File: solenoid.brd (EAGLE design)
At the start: 76.2 x 25.4 mm, 41 parts, among them Y1 ECS-80-S-4X

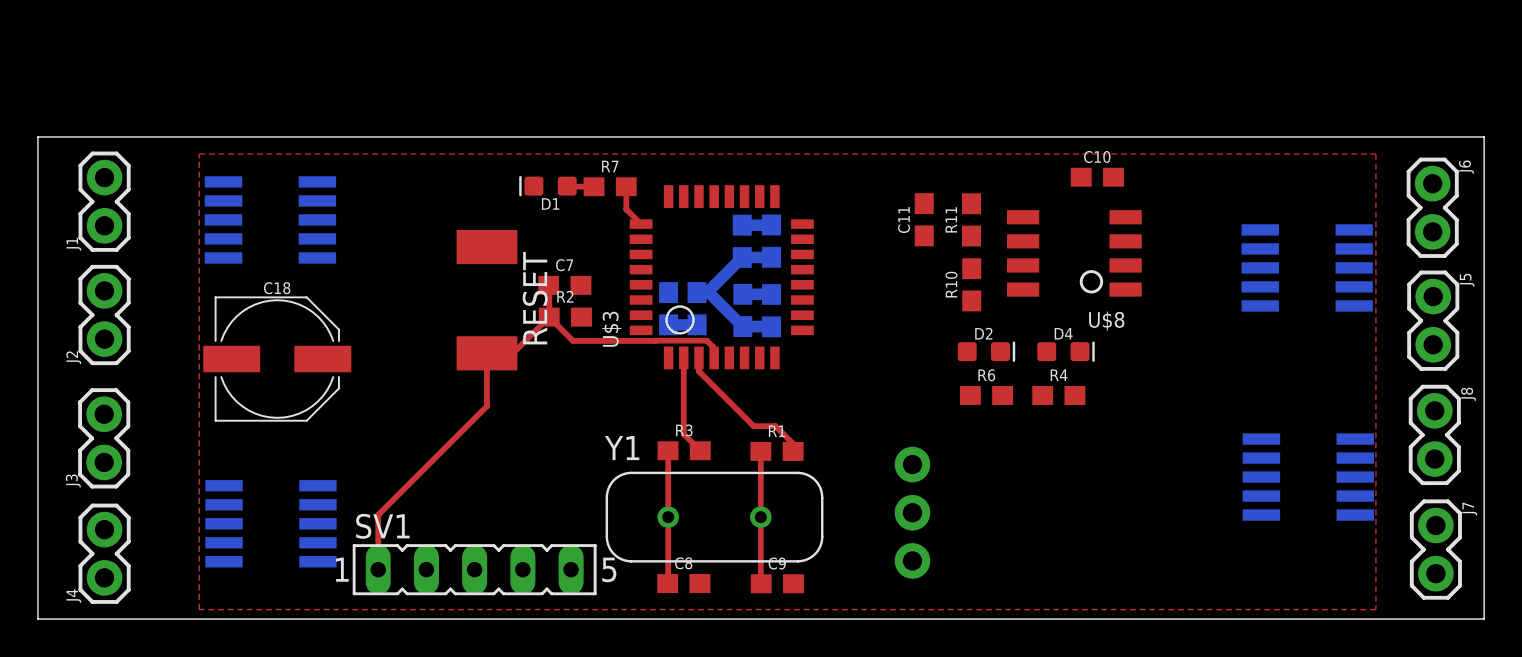
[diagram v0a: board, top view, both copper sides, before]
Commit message: Newly sized board w/ schematic changes
This is the first attempt at routing the 1.2" by  1.4" solenoid board with a removed h-bridge and with some questions as to some airwires
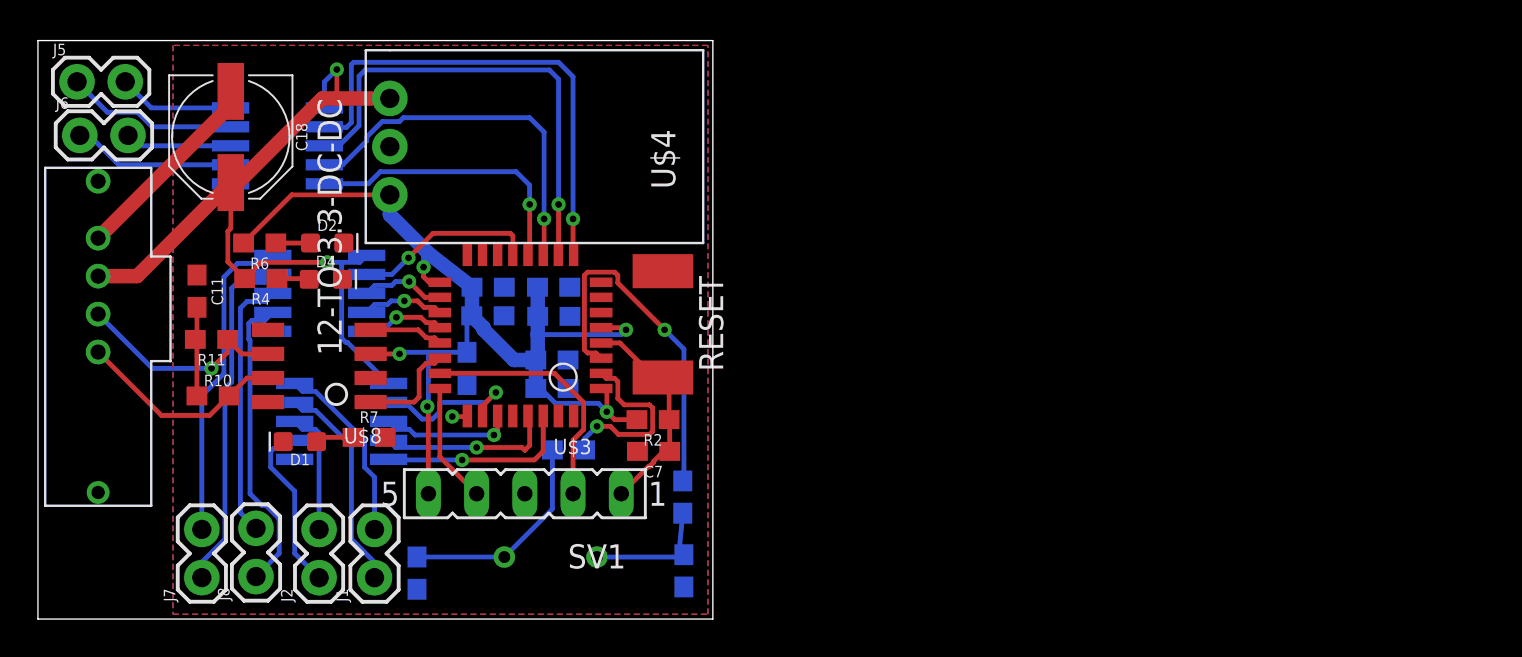
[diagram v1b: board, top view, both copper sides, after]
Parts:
- removed J3, J4: (no value), SparkFun-Connectors:1X02
- removed U$2: LV8548M, HBridge:SOP100P600X175-10N
- added U$7: T2I, BackplaneParts:T2I
- moved J5 72.4 mm to (2.06, 28.3), turned to 0 degrees
- moved J6 71.3 mm to (2.21, 25.5), turned to 0 degrees
- moved J7 65.1 mm to (8.64, 2.18), turned to 90 degrees
- moved J8 62.7 mm to (11.5, 2.24), turned to 90 degrees
- moved U$5 54.6 mm to (12.6, 24.9), turned to 0 degrees
- moved U$6 53.0 mm to (14.8, 17.2), turned to 0 degrees
- moved R4 42.5 mm to (11.7, 17.9), turned to 180 degrees
- moved R11 40.5 mm to (9.14, 14.7), turned to 180 degrees
- moved R10 40.4 mm to (9.23, 11.8), turned to 0 degrees
- moved U$8 40.2 mm to (17.5, 15.2)
- moved R6 39.1 mm to (11.7, 19.8), turned to 180 degrees
- moved D4 39.0 mm to (15.2, 17.9)
- moved C11 38.5 mm to (8.38, 17.3), turned to 270 degrees
- moved D2 35.1 mm to (15.2, 19.8)
- moved C10 34.7 mm to (22.6, 13.2), flipped to the bottom, turned to 270 degrees
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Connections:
- removed net GPIO4: U$2.IN1, U$3.PB5
- removed net GPIO5: U$2.IN2, U$3.PA0
- removed net GPIO6: U$2.IN3, U$3.PA1
- removed net GPIO7: U$2.IN4, U$3.PA2
- removed net SOL3_1: J3.2, U$2.OUT1
- removed net SOL3_2: J3.1, U$2.OUT2
- removed net SOL4_1: J4.2, U$2.OUT3
- removed net SOL4_2: J4.1, U$2.OUT4
- net 12V: now also U$7.3; no longer U$2.VCC
- net CAN_H: now also U$7.1
- net CAN_L: now also U$7.2
- net GND: now also U$7.4; no longer U$2.GND
- net GPIO0: now also U$1.IN4; no longer U$1.IN1
- net GPIO1: now also U$1.IN3; no longer U$1.IN2
- net GPIO2: now also U$1.IN2; no longer U$1.IN3
- net GPIO3: now also U$1.IN1; no longer U$1.IN4
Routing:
- net +3V3: track 9.36 -> 57.6 mm, vias 0 -> 5
- net 12V: track 0.00 -> 43.0 mm, vias 0 -> 2
- net GPIO8: track 0.00 -> 26.0 mm, vias 0 -> 1
- net GPIO9: track 0.00 -> 25.0 mm, vias 0 -> 1
- net GPIO10: track 0.00 -> 19.5 mm, vias 0 -> 1
- net SOL7_2: track 0.00 -> 18.4 mm
- net NRST: track 29.4 -> 11.6 mm
- net SOL7_1: track 0.00 -> 16.8 mm
- net SOL8_2: track 0.00 -> 16.1 mm
- net GPIO11: track 0.00 -> 15.1 mm, vias 0 -> 1
- net SOL8_1: track 0.00 -> 14.0 mm
- net SWDIO: track 0.00 -> 13.3 mm
- net OSC_OUT: track 7.65 -> 19.2 mm, vias 0 -> 1
- net CAN_L: track 0.00 -> 11.5 mm, vias 0 -> 1
- net SOL1_2: track 0.00 -> 11.4 mm
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- added copper zone on layer 16, net GND
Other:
- board size 76.2 x 25.4 mm -> 35.6 x 30.5 mm

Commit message: last version of this board
abandon all hope of this first draft. It passed DRC for default but not the DRC for ECE Senior Design have to scrap this idea :(
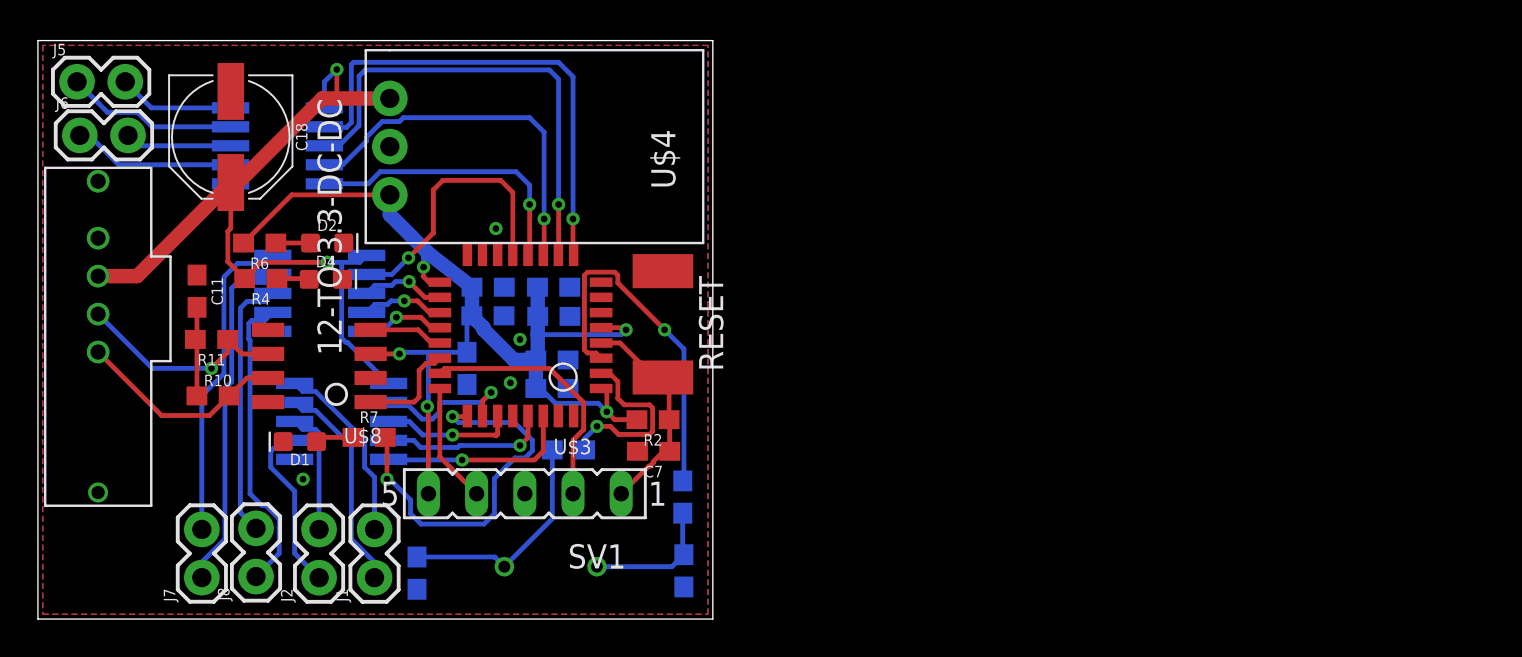
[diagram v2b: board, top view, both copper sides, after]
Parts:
- moved Y1 0.51 mm to (27.0, 2.76)
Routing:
- net LED: track 1.15 -> 20.1 mm, vias 1 -> 2
- net GND: track 10.6 -> 0.00 mm, vias 0 -> 4
- net GPIO12: track 9.64 -> 14.6 mm
- net N$2: track 11.3 -> 12.0 mm

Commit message: Clearance issues fixed
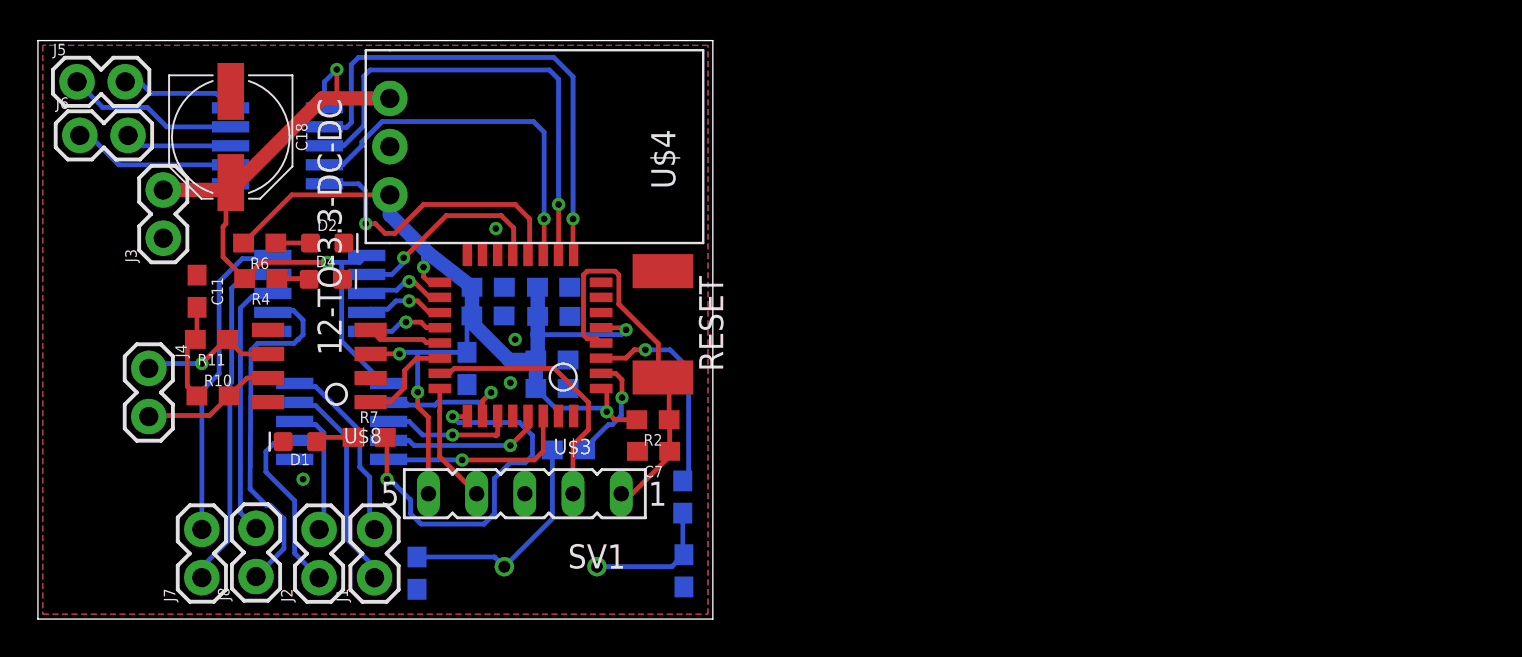
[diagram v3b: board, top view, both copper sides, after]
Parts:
- removed U$7: T2I, BackplaneParts:T2I
- added J3, J4: (no value), SparkFun-Connectors:1X02
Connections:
- net 12V: now also J3.2; no longer U$7.3
- net CAN_H: now also J4.2; no longer U$7.1
- net CAN_L: now also J4.1; no longer U$7.2
- net GND: now also J3.1; no longer U$7.4
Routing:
- net NRST: track 11.6 -> 20.4 mm
- net OSC_OUT: track 19.2 -> 11.3 mm
- net 12V: track 43.0 -> 37.8 mm
- net CAN_L: track 11.5 -> 7.23 mm
- net CAN_H: track 11.2 -> 7.13 mm
- net OSC_IN: track 9.91 -> 5.90 mm
- net GPIO12: track 14.6 -> 10.9 mm
- net SOL8_2: track 16.1 -> 18.5 mm
- net GPIO3: track 8.06 -> 7.23 mm
- net GPIO11: track 15.1 -> 15.8 mm

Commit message: Update solenoid.brd
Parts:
- moved J5 26.0 mm to (2.43, 2.31), turned to 90 degrees
- moved J6 20.8 mm to (5.51, 4.91), turned to 270 degrees
- moved U$5 0.76 mm to (11.9, 24.9)
- moved RESET 0.25 mm to (32.9, 15.8)
- moved J3 0.25 mm to (6.35, 20.1)
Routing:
- net SOL5_1: track 6.12 -> 30.9 mm
- net SOL6_1: track 5.63 -> 30.4 mm
- net SOL5_2: track 9.07 -> 32.6 mm
- net SOL6_2: track 8.58 -> 25.8 mm
- net GPIO10: track 19.3 -> 18.0 mm
- net OSC_OUT: track 11.3 -> 12.5 mm
- net SWCLK: track 6.36 -> 7.57 mm
- net GPIO9: track 25.0 -> 25.7 mm
- net +3V3: track 57.9 -> 58.5 mm
- net GPIO8: track 26.2 -> 26.8 mm
- net GPIO11: track 15.8 -> 16.3 mm

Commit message: Update solenoid.brd
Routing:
- net GND: track 0.00 -> 7.00 mm
- net SOL8_2: track 18.5 -> 20.4 mm
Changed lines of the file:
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@@
 <via x="24.13" y="20.574" extent="1-16" drill="0.35"/>
 <via x="25.146" y="14.732" extent="1-16" drill="0.35"/>
+<contactref element="J3" pad="1"/>
+<via x="13.97" y="15.24" extent="1-16" drill="0.35"/>
 <via x="24.892" y="12.446" extent="1-16" drill="0.35"/>
-<contactref element="J3" pad="1"/>
-<via x="14.478" y="16.51" extent="1-16" drill="0.35"/>
-<wire x1="14.478" y1="16.51" x2="12.3746" y2="15.158" width="0" layer="19" extent="16-16"/>
-<wire x1="22.606" y1="12.358" x2="24.892" y2="12.446" width="0" layer="19" extent="16-16"/>
+<wire x1="24.892" y1="12.446" x2="27.178" y2="12.446" width="0.2032" layer="1"/>
+<wire x1="28.224" y1="11.4" x2="28.224" y2="10.698" width="0.2032" layer="1"/>
+<wire x1="27.178" y1="12.446" x2="28.224" y2="11.4" width="0.2032" layer="1"/>
+<wire x1="24.892" y1="12.446" x2="24.638" y2="12.7" width="0.254" layer="16"/>
+<wire x1="24.638" y1="12.7" x2="22.948" y2="12.7" width="0.254" layer="16"/>
+<wire x1="22.948" y1="12.7" x2="22.606" y2="12.358" width="0.254" layer="16"/>
+<wire x1="28.022" y1="17.484" x2="32.931" y2="18.584" width="0" layer="19" extent="1-16"/>
+<wire x1="28.032" y1="15.946" x2="28.022" y2="17.484" width="0" layer="19" extent="16-16"/>
+<wire x1="27.934" y1="13.648" x2="28.032" y2="15.946" width="0" layer="19" extent="16-16"/>
+<wire x1="27.934" y1="12.148" x2="27.934" y2="13.648" width="0" layer="19" extent="16-16"/>
+<wire x1="28.224" y1="10.698" x2="27.934" y2="12.148" width="0" layer="19" extent="1-16"/>
+<wire x1="27.424" y1="10.698" x2="28.224" y2="10.698" width="0" layer="19" extent="1-1"/>
+<wire x1="25.146" y1="14.732" x2="24.638" y2="12.7" width="0" layer="19" extent="1-1"/>
+<wire x1="24.56" y1="15.976" x2="25.146" y2="14.732" width="0" layer="19" extent="16-16"/>
+<wire x1="24.57" y1="17.484" x2="24.56" y2="15.976" width="0" layer="19" extent="16-16"/>
+<wire x1="22.624" y1="19.198" x2="24.57" y2="17.484" width="0" layer="19" extent="1-16"/>
+<wire x1="24.13" y1="20.574" x2="22.624" y2="19.198" width="0" layer="19" extent="1-1"/>
+<wire x1="31.588" y1="8.836" x2="28.224" y2="10.698" width="0" layer="19" extent="1-1"/>
+<wire x1="25.654" y1="6.604" x2="27.424" y2="10.698" width="0" layer="19" extent="1-1"/>
+<wire x1="17.526" y1="12.7" x2="22.606" y2="12.358" width="0" layer="19" extent="1-16"/>
+<wire x1="13.97" y1="15.24" x2="17.526" y2="12.7" width="0" layer="19" extent="1-1"/>
+<wire x1="12.3746" y1="15.158" x2="13.97" y2="15.24" width="0" layer="19" extent="16-16"/>
+<wire x1="16.045" y1="17.9" x2="13.97" y2="15.24" width="0" layer="19" extent="1-1"/>
+<wire x1="16.117" y1="19.812" x2="16.045" y2="17.9" width="0" layer="19" extent="1-1"/>
+<wire x1="8.382" y1="18.122" x2="12.3746" y2="15.158" width="0" layer="19" extent="1-16"/>
+<wire x1="6.35" y1="20.066" x2="8.382" y2="18.122" width="0" layer="19" extent="1-1"/>
+<wire x1="9.3866" y1="22.934" x2="6.35" y2="20.066" width="0" layer="19" extent="16-16"/>
+<wire x1="10.16" y1="27.8" x2="9.3866" y2="22.934" width="0" layer="19" extent="1-16"/>
+<wire x1="18.542" y1="24.892" x2="16.117" y2="19.812" width="0" layer="19" extent="1-1"/>
+<wire x1="12.925" y1="9.348" x2="17.526" y2="12.7" width="0" layer="19" extent="1-1"/>
+<wire x1="13.5286" y1="8.414" x2="12.925" y2="9.348" width="0" layer="19" extent="1-16"/>
+<wire x1="13.97" y1="7.366" x2="13.5286" y2="8.414" width="0" layer="19" extent="16-16"/>
+<wire x1="34.036" y1="1.69" x2="31.588" y2="8.836" width="0" layer="19" extent="1-16"/>
+<wire x1="19.974" y1="1.569" x2="25.654" y2="6.604" width="0" layer="19" extent="16-16"/>
 </signal>
 <signal name="+3V3">
@@
 <wire x1="11.177796875" y1="6.856203125" x2="11.229965625" y2="14.172671875" width="0.254" layer="16"/>
 <wire x1="12.9632" y1="5.2830125" x2="12.9632" y2="3.7112" width="0.254" layer="16"/>
-<wire x1="13.97" y1="15.748" x2="13.462" y2="16.256" width="0.254" layer="16"/>
-<wire x1="13.462" y1="16.256" x2="12.954" y2="16.256" width="0.254" layer="16"/>
 <wire x1="11.229965625" y1="14.172671875" x2="11.58554375" y2="14.52825" width="0.254" layer="16"/>
-<wire x1="11.58554375" y1="14.52825" x2="13.495625" y2="14.52825" width="0.254" layer="16"/>
-<wire x1="13.699375" y1="14.732" x2="13.716" y2="14.732" width="0.254" layer="16"/>
-<wire x1="13.495625" y1="14.52825" x2="13.699375" y2="14.732" width="0.254" layer="16"/>
-<wire x1="13.716" y1="14.732" x2="13.97" y2="14.986" width="0.254" layer="16"/>
-<wire x1="13.97" y1="14.986" x2="13.97" y2="15.748" width="0.254" layer="16"/>
-<wire x1="12.954" y1="16.256" x2="12.3746" y2="16.158" width="0" layer="19" extent="16-16"/>
+<wire x1="14.27425" y1="14.52825" x2="14.732" y2="14.986" width="0.254" layer="16"/>
+<wire x1="14.732" y1="14.986" x2="14.732" y2="15.494" width="0.254" layer="16"/>
+<wire x1="14.068" y1="16.158" x2="12.3746" y2="16.158" width="0.254" layer="16"/>
+<wire x1="11.58554375" y1="14.52825" x2="14.27425" y2="14.52825" width="0.254" layer="16"/>
+<wire x1="14.732" y1="15.494" x2="14.068" y2="16.158" width="0.254" layer="16"/>
 </signal>
 <signal name="SOL8_1">

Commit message: Update solenoid.brd
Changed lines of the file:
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@@
 <wire x1="24.638" y1="12.7" x2="22.948" y2="12.7" width="0.254" layer="16"/>
 <wire x1="22.948" y1="12.7" x2="22.606" y2="12.358" width="0.254" layer="16"/>
-<wire x1="28.022" y1="17.484" x2="32.931" y2="18.584" width="0" layer="19" extent="1-16"/>
-<wire x1="28.032" y1="15.946" x2="28.022" y2="17.484" width="0" layer="19" extent="16-16"/>
-<wire x1="27.934" y1="13.648" x2="28.032" y2="15.946" width="0" layer="19" extent="16-16"/>
-<wire x1="27.934" y1="12.148" x2="27.934" y2="13.648" width="0" layer="19" extent="16-16"/>
-<wire x1="28.224" y1="10.698" x2="27.934" y2="12.148" width="0" layer="19" extent="1-16"/>
-<wire x1="27.424" y1="10.698" x2="28.224" y2="10.698" width="0" layer="19" extent="1-1"/>
-<wire x1="25.146" y1="14.732" x2="24.638" y2="12.7" width="0" layer="19" extent="1-1"/>
-<wire x1="24.56" y1="15.976" x2="25.146" y2="14.732" width="0" layer="19" extent="16-16"/>
-<wire x1="24.57" y1="17.484" x2="24.56" y2="15.976" width="0" layer="19" extent="16-16"/>
-<wire x1="22.624" y1="19.198" x2="24.57" y2="17.484" width="0" layer="19" extent="1-16"/>
-<wire x1="24.13" y1="20.574" x2="22.624" y2="19.198" width="0" layer="19" extent="1-1"/>
-<wire x1="31.588" y1="8.836" x2="28.224" y2="10.698" width="0" layer="19" extent="1-1"/>
-<wire x1="25.654" y1="6.604" x2="27.424" y2="10.698" width="0" layer="19" extent="1-1"/>
-<wire x1="17.526" y1="12.7" x2="22.606" y2="12.358" width="0" layer="19" extent="1-16"/>
-<wire x1="13.97" y1="15.24" x2="17.526" y2="12.7" width="0" layer="19" extent="1-1"/>
-<wire x1="12.3746" y1="15.158" x2="13.97" y2="15.24" width="0" layer="19" extent="16-16"/>
-<wire x1="16.045" y1="17.9" x2="13.97" y2="15.24" width="0" layer="19" extent="1-1"/>
-<wire x1="16.117" y1="19.812" x2="16.045" y2="17.9" width="0" layer="19" extent="1-1"/>
-<wire x1="8.382" y1="18.122" x2="12.3746" y2="15.158" width="0" layer="19" extent="1-16"/>
-<wire x1="6.35" y1="20.066" x2="8.382" y2="18.122" width="0" layer="19" extent="1-1"/>
-<wire x1="9.3866" y1="22.934" x2="6.35" y2="20.066" width="0" layer="19" extent="16-16"/>
-<wire x1="10.16" y1="27.8" x2="9.3866" y2="22.934" width="0" layer="19" extent="1-16"/>
-<wire x1="18.542" y1="24.892" x2="16.117" y2="19.812" width="0" layer="19" extent="1-1"/>
-<wire x1="12.925" y1="9.348" x2="17.526" y2="12.7" width="0" layer="19" extent="1-1"/>
-<wire x1="13.5286" y1="8.414" x2="12.925" y2="9.348" width="0" layer="19" extent="1-16"/>
-<wire x1="13.97" y1="7.366" x2="13.5286" y2="8.414" width="0" layer="19" extent="16-16"/>
-<wire x1="34.036" y1="1.69" x2="31.588" y2="8.836" width="0" layer="19" extent="1-16"/>
-<wire x1="19.974" y1="1.569" x2="25.654" y2="6.604" width="0" layer="19" extent="16-16"/>
 </signal>
 <signal name="+3V3">
@@
 <contactref element="Y1" pad="1"/>
 <contactref element="R3" pad="1"/>
-<wire x1="24.574" y1="2.758" x2="24.063" y2="3.269" width="0.254" layer="16"/>
-<wire x1="24.063" y1="3.269" x2="19.974" y2="3.269" width="0.254" layer="16"/>
+<wire x1="24.574" y1="2.758" x2="22.288" y2="2.758" width="0.254" layer="16"/>
+<wire x1="22.288" y1="2.758" x2="21.777" y2="3.269" width="0.254" layer="16"/>
+<wire x1="21.777" y1="3.269" x2="19.974" y2="3.269" width="0.254" layer="16"/>
 <wire x1="27.104" y1="8.91" x2="27.104" y2="5.288" width="0.254" layer="16"/>
 <wire x1="27.104" y1="5.288" x2="24.574" y2="2.758" width="0.254" layer="16"/>

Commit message: Update solenoid.brd
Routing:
- net +3V3: track 58.5 -> 59.1 mm
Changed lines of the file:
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@@
 <wire x1="30.988" y1="15.24" x2="30.734" y2="14.986" width="0.254" layer="16"/>
 <wire x1="30.734" y1="14.986" x2="26.332" y2="14.986" width="0.254" layer="16"/>
-<wire x1="18.542" y1="22.352" x2="13.374" y2="22.352" width="0.254" layer="1"/>
-<wire x1="13.374" y1="22.352" x2="10.834" y2="19.812" width="0.254" layer="1"/>
 <via x="20.0084" y="11.95728125" extent="1-16" drill="0.35"/>
 <wire x1="22.86" y1="15.976" x2="22.606" y2="15.722" width="0.254" layer="16"/>
@@
 <wire x1="19.2464" y1="11.19528125" x2="19.2464" y2="7.9316" width="0.254" layer="1"/>
 <wire x1="19.2464" y1="7.9316" x2="20.574" y2="6.604" width="0.254" layer="1"/>
+<wire x1="10.834" y1="19.812" x2="10.834" y2="20.74" width="0.254" layer="1"/>
+<wire x1="10.834" y1="20.74" x2="12.446" y2="22.352" width="0.254" layer="1"/>
+<wire x1="12.446" y1="22.352" x2="18.542" y2="22.352" width="0.254" layer="1"/>
 </signal>
 <signal name="GPIO1">
